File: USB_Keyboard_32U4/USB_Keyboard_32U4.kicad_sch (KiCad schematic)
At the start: 11 parts, among them J1 USB_C_Receptacle_USB2.0_16P, U1 ATmega32U4-A, Y1 16mhz

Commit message: Update keyboard PCB footprints to 0805
This commit updates the USB keyboard board from 0201/0603 passive packages to 0805 hand-solder footprints for the LEDs and resistors. It repositions the affected components, refreshes the KiCad project metadata, and adjusts the board outline and routed tracks to match the larger parts. It also includes the generated production .DS_Store artifact.
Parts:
- D1, D2: footprint LED_SMD:LED_0201_0603Metric -> LED_SMD:LED_0805_2012Metric_Pad1.15x1.40mm_HandSolder
- R1, R2, R3, R4, R5, R6: footprint Resistor_SMD:R_0603_1608Metric -> Resistor_SMD:R_0805_2012Metric_Pad1.20x1.40mm_HandSolder
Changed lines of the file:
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@@
 			)
 		)
-		(property "Footprint" "Resistor_SMD:R_0603_1608Metric"
+		(property "Footprint" "Resistor_SMD:R_0805_2012Metric_Pad1.20x1.40mm_HandSolder"
 			(at 120.65 81.788 90)
 			(hide yes)
@@
 			)
 		)
-		(property "Footprint" "LED_SMD:LED_0201_0603Metric"
+		(property "Footprint" "LED_SMD:LED_0805_2012Metric_Pad1.15x1.40mm_HandSolder"
 			(at 110.49 58.42 0)
 			(hide yes)
@@
 			)
 		)
-		(property "Footprint" "Resistor_SMD:R_0603_1608Metric"
+		(property "Footprint" "Resistor_SMD:R_0805_2012Metric_Pad1.20x1.40mm_HandSolder"
 			(at 110.49 90.678 90)
 			(hide yes)
@@
 			)
 		)
-		(property "Footprint" "Resistor_SMD:R_0603_1608Metric"
+		(property "Footprint" "Resistor_SMD:R_0805_2012Metric_Pad1.20x1.40mm_HandSolder"
 			(at 102.362 67.31 90)
 			(hide yes)
@@
 			)
 		)
-		(property "Footprint" "Resistor_SMD:R_0603_1608Metric"
+		(property "Footprint" "Resistor_SMD:R_0805_2012Metric_Pad1.20x1.40mm_HandSolder"
 			(at 110.49 95.758 90)
 			(hide yes)
@@
 			)
 		)
-		(property "Footprint" "LED_SMD:LED_0201_0603Metric"
+		(property "Footprint" "LED_SMD:LED_0805_2012Metric_Pad1.15x1.40mm_HandSolder"
 			(at 179.07 114.3 0)
 			(hide yes)
@@
 			)
 		)
-		(property "Footprint" "Resistor_SMD:R_0603_1608Metric"
+		(property "Footprint" "Resistor_SMD:R_0805_2012Metric_Pad1.20x1.40mm_HandSolder"
 			(at 120.65 79.248 90)
 			(hide yes)
@@
 			)
 		)
-		(property "Footprint" "Resistor_SMD:R_0603_1608Metric"
+		(property "Footprint" "Resistor_SMD:R_0805_2012Metric_Pad1.20x1.40mm_HandSolder"
 			(at 172.72 108.458 90)
 			(hide yes)

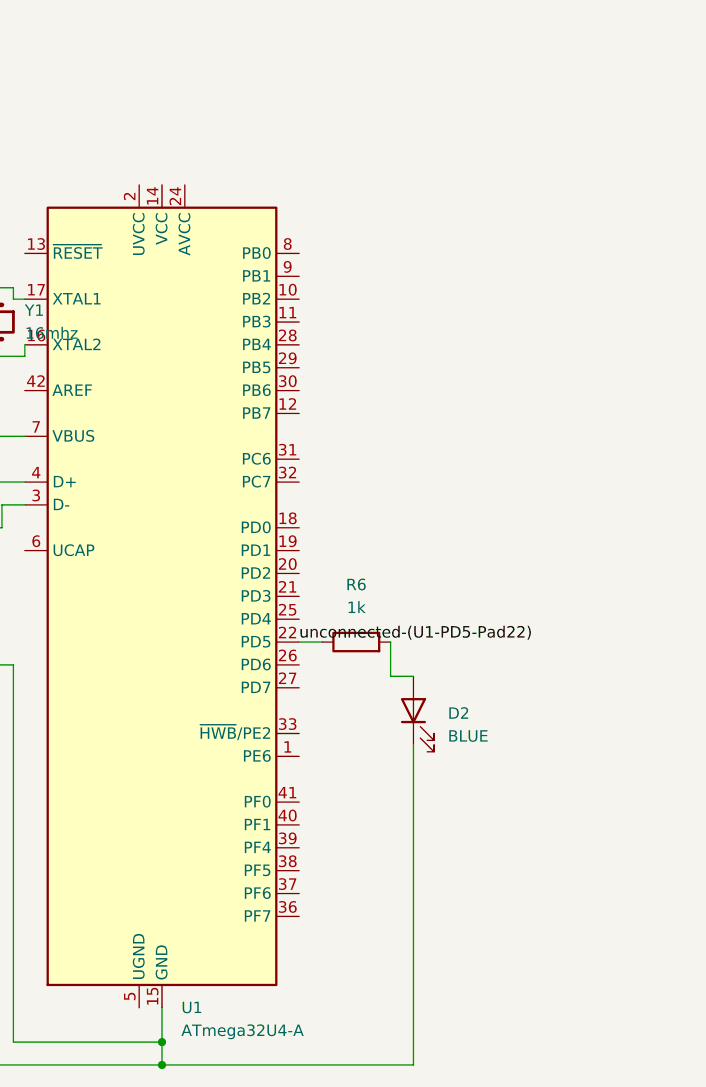
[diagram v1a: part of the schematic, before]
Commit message: Edited some pcb layout
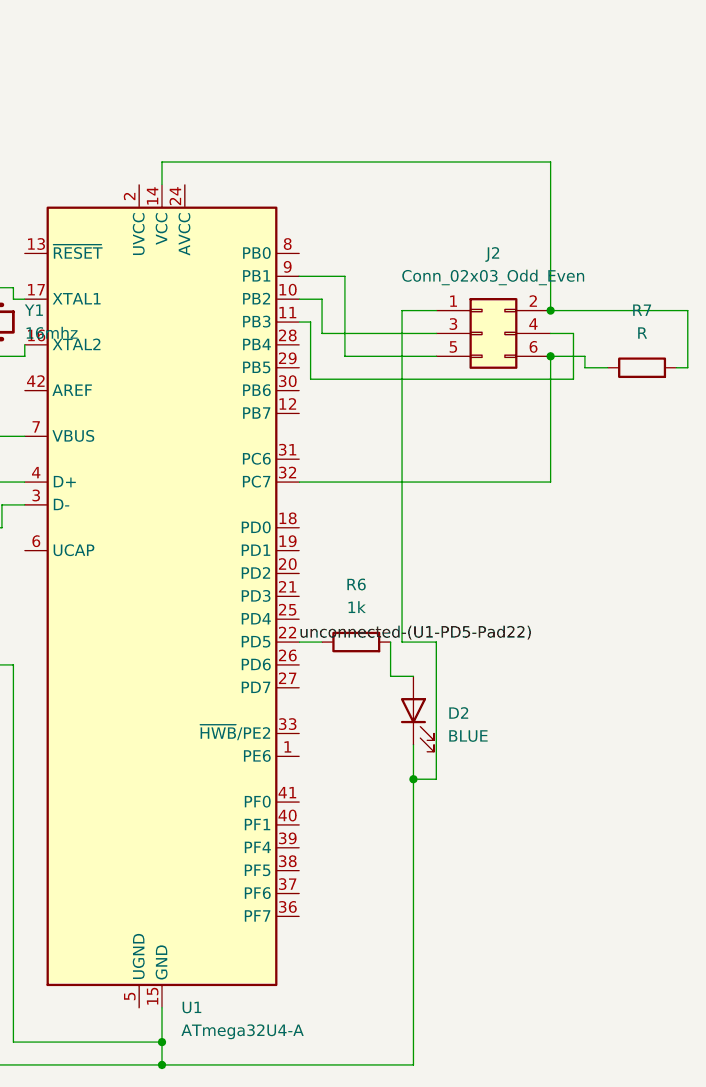
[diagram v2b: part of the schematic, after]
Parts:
- added J2: Conn_02x03_Odd_Even, Connector_PinHeader_2.54mm:PinHeader_2x03_P2.54mm_Vertical, symbol Connector_Generic:Conn_02x03_Odd_Even
- added R7: R, Resistor_SMD:R_0805_2012Metric_Pad1.20x1.40mm_HandSolder, symbol Device:R
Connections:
- net Net-(J1-GND-PadA1): now also J2.1 (Pin_1)
- net at U1.10 (PB2): now also J2.3 (Pin_3)
- net at U1.11 (PB3): now also J2.4 (Pin_4)
- net at U1.14 (VCC), U1.34 (VCC): now also J2.2 (Pin_2), R7.2
- net at U1.32 (PC7): now also J2.6 (Pin_6), R7.1
- net at U1.9 (PB1): now also J2.5 (Pin_5)

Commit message: Updated schematic, pcb and bom.
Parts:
- removed Y1: 16mhz, Crystal:Crystal_SMD_3225-4Pin_3.2x2.5mm, symbol Device:Crystal
- added C1, C2: 27pF, Capacitor_SMD:C_0603_1608Metric_Pad1.08x0.95mm_HandSolder, symbol Device:C
- added C3, C4, C5, C6, C9: 100nF, Capacitor_SMD:C_0603_1608Metric_Pad1.08x0.95mm_HandSolder, symbol Device:C
- added C7: 10uF, Capacitor_SMD:C_0603_1608Metric_Pad1.08x0.95mm_HandSolder, symbol Device:C
- added C8: 1uF, Capacitor_SMD:C_0603_1608Metric_Pad1.08x0.95mm_HandSolder, symbol Device:C
- added Y1: 16MHz, Crystal:Crystal_SMD_3225-4Pin_3.2x2.5mm, symbol Device:Crystal_GND24
- D1, D2: footprint LED_SMD:LED_0805_2012Metric_Pad1.15x1.40mm_HandSolder -> LED_SMD:LED_0603_1608Metric_Pad1.05x0.95mm_HandSolder
- J2: footprint Connector_PinHeader_2.54mm:PinHeader_2x03_P2.54mm_Vertical -> 2x3 Pads:MicroKey_AVR_ISP_2x3_SMD
- R1, R2, R3, R4, R5, R6: footprint Resistor_SMD:R_0805_2012Metric_Pad1.20x1.40mm_HandSolder -> Resistor_SMD:R_0603_1608Metric_Pad0.98x0.95mm_HandSolder
- R7: value R -> 10k; footprint Resistor_SMD:R_0805_2012Metric_Pad1.20x1.40mm_HandSolder -> Resistor_SMD:R_0603_1608Metric_Pad0.98x0.95mm_HandSolder
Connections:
- net VCC: now reaches J2.2 (Pin_2), U1.14 (VCC), U1.34 (VCC)
- net VCC: now also J1.A4 (VBUS), J1.A9 (VBUS), J1.B4 (VBUS), J1.B9 (VBUS), R5.1, R7.1, U1.2 (UVCC), U1.24 (AVCC), U1.44 (AVCC), U1.7 (VBUS), C3.1, C4.1, C5.1, C6.1, C7.1; no longer R7.2
- net at J1.A6 (D+), R4.1: now also J1.B6 (D+)
- net at J1.A7 (D-), R3.1: now also J1.B7 (D-)
- net GND: now reaches J1.SH (SHIELD)
- net GND: now also D1.2 (A), D2.1 (K), J1.A1 (GND), J1.A12 (GND), J1.B1 (GND), J1.B12 (GND), J2.1 (Pin_1), R1.2, R2.2, U1.15 (GND), U1.23 (GND), U1.35 (GND), U1.43 (GND), U1.5 (UGND), C1.1, C2.1, C3.2, C4.2, C5.2, C6.2, C7.2, C8.2, C9.2, Y1.2, Y1.4
- net D+: now reaches U1.4 (D+)
- net D+: now also R4.2; no longer R3.2
- net at U1.17 (XTAL1): now also C1.2, Y1.1
- net at U1.16 (XTAL2): now also C2.2, Y1.3
- net PB2: now reaches J2.3 (Pin_3), U1.10 (PB2)
- net PB3: now reaches J2.4 (Pin_4), U1.11 (PB3)
- net RESET: now reaches U1.13 (~{RESET})
- net RESET: now also J2.6 (Pin_6), R7.2
- net D-: now reaches U1.3 (D-)
- net D-: now also R3.2; no longer R4.2
- net at U1.42 (AREF): now also C9.1
- net at U1.6 (UCAP): now also C8.1
- net PB1: now reaches J2.5 (Pin_5), U1.9 (PB1)
- removed net Net-(J1-GND-PadA1): D1.1 (K), D2.1 (K), J1.A1 (GND), J1.A12 (GND), J1.B1 (GND), J1.B12 (GND), J2.1 (Pin_1), R1.2, R2.2, U1.15 (GND), U1.23 (GND), U1.35 (GND), U1.43 (GND)
- net unconnected-(U1-PD5-Pad22): no longer names the net of R6.1, U1.22 (PD5)
- new net: D1.1 (K), R5.2
- now unconnected: U1.32 (PC7)

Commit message: Added a folder with finished files.
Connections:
- net GND: now also D1.1 (K); no longer D1.2 (A)
- net at R5.2: now also D1.2 (A); no longer D1.1 (K)
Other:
- moved on the sheet: D1
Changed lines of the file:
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@@
 	(symbol
 		(lib_id "Device:LED")
-		(at 86.36 72.39 90)
+		(at 86.36 72.39 270)
 		(unit 1)
 		(body_style 1)

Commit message: Finalize PCB layout for fabrication
Move the ISP pogo pads to the board underside, add manufacturing-adjusted USB-C and ISP footprints, and refine routing, outline, silkscreen, and design rules. Remove intermediate layout files while retaining final-board verification and relocation records.
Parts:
- J1: footprint Connector_USB:USB_C_Receptacle_GCT_USB4105-xx-A_16P_TopMnt_Horizontal -> MicroKey_Local:USB4105_JLC_0p20mm_NPTH_Clearance
- J2: footprint 2x3 Pads:MicroKey_AVR_ISP_2x3_SMD -> MicroKey_Local:AVR_ISP_2x3_Pogo_3p23x1p80
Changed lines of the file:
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@@
 			)
 		)
-		(property "Footprint" "Connector_USB:USB_C_Receptacle_GCT_USB4105-xx-A_16P_TopMnt_Horizontal"
+		(property "Footprint" "MicroKey_Local:USB4105_JLC_0p20mm_NPTH_Clearance"
 			(at 74.93 99.06 0)
 			(hide yes)
@@
 			)
 		)
-		(property "Footprint" "2x3 Pads:MicroKey_AVR_ISP_2x3_SMD"
+		(property "Footprint" "MicroKey_Local:AVR_ISP_2x3_Pogo_3p23x1p80"
 			(at 218.44 90.17 0)
 			(hide yes)

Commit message: Update USB-C connector footprint
Replace the USB-C receptacle footprint with the GCT_USB4105-GF-A and update its PCB placement. Refresh the BOM, README, and production outputs to match.
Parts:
- J1: footprint MicroKey_Local:USB4105_JLC_0p20mm_NPTH_Clearance -> Custom Footprints:GCT_USB4105-GF-A
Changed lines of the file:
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@@
 			)
 		)
-		(property "Footprint" "MicroKey_Local:USB4105_JLC_0p20mm_NPTH_Clearance"
+		(property "Footprint" "Custom Footprints:GCT_USB4105-GF-A"
 			(at 74.93 99.06 0)
 			(hide yes)
